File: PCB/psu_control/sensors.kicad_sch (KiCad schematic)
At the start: 35 parts

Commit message: psu_control v4 is completed
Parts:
- C11, C12, C13, C14, C15, C16: renamed from C?; footprint (none) -> Capacitor_SMD:C_0805_2012Metric
- J11, J12, J13, J14: renamed from J?; footprint (none) -> Connector_JST:JST_PH_B3B-PH-K_1x03_P2.00mm_Vertical
- R25, R26: renamed from R?; value R -> 10k; footprint (none) -> Resistor_SMD:R_0805_2012Metric
- R27, R28, R29, R30, R31, R32, R33, R34, R35, R36: renamed from R?; footprint (none) -> Resistor_SMD:R_0805_2012Metric
- SW2, SW3, SW4, SW5, SW6: renamed from SW?; footprint (none) -> Connector_JST:JST_PH_B2B-PH-K_1x02_P2.00mm_Vertical
- TH1: renamed from TH?; footprint (none) -> Connector_JST:JST_PH_B2B-PH-K_1x02_P2.00mm_Vertical
- TH2: renamed from TH?; footprint (none) -> Resistor_SMD:R_0805_2012Metric
- U5: renamed from U?; footprint (none) -> Package_SO:TSSOP-14_4.4x5mm_P0.65mm
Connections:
- net BUTTON_OTHER: now also U5.6; no longer U5.10
- net BUTTON_START: now also U5.10; no longer U5.2
- net BUTTON_STOP: now also U5.8; no longer U5.4
- net BUTTON_VOLUME_DOWN: now also U5.4; no longer U5.8
- net BUTTON_VOLUME_UP: now also U5.2; no longer U5.6
- net GND: now also SW2.1 (A), SW3.1 (A), SW4.1 (A), SW5.1 (A), SW6.1 (A); no longer SW2.2 (B), SW3.2 (B), SW4.2 (B), SW5.2 (B), SW6.2 (B)
- net at R27.2, R30.1: now also SW2.2 (B); no longer SW2.1 (A)
- net at C11.1, R30.2: now also U5.11; no longer U5.1
- net at R34.2, R36.1: now also SW6.2 (B); no longer SW6.1 (A)
- net at R28.2, R31.1: now also SW3.2 (B); no longer SW3.1 (A)
- net at C12.1, R31.2: now also U5.9; no longer U5.3
- net at R33.2, R35.1: now also SW5.2 (B); no longer SW5.1 (A)
- net at C15.1, R35.2: now also U5.3; no longer U5.9
- net at C16.1, R36.2: now also U5.5; no longer U5.11
- net at R29.2, R32.1: now also SW4.2 (B); no longer SW4.1 (A)
- net at C13.1, R32.2: now also U5.1; no longer U5.5
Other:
- note added: "J11: JST PH Connector J12: JST PH Connector J13: JST PH Connector J14: JST PH Connector"
- note added: "SW2: JST PH Connector SW3: JST PH Connector SW4: JST PH Connector SW5: JST PH Connector SW6: JST PH Connector"
- note added: "TH1: JST PH Connector TH2: 0805 SMD"
- moved on the sheet: C12, C16, J11, J13, J14, R28, R31, R34, R36, SW2, SW3, SW4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

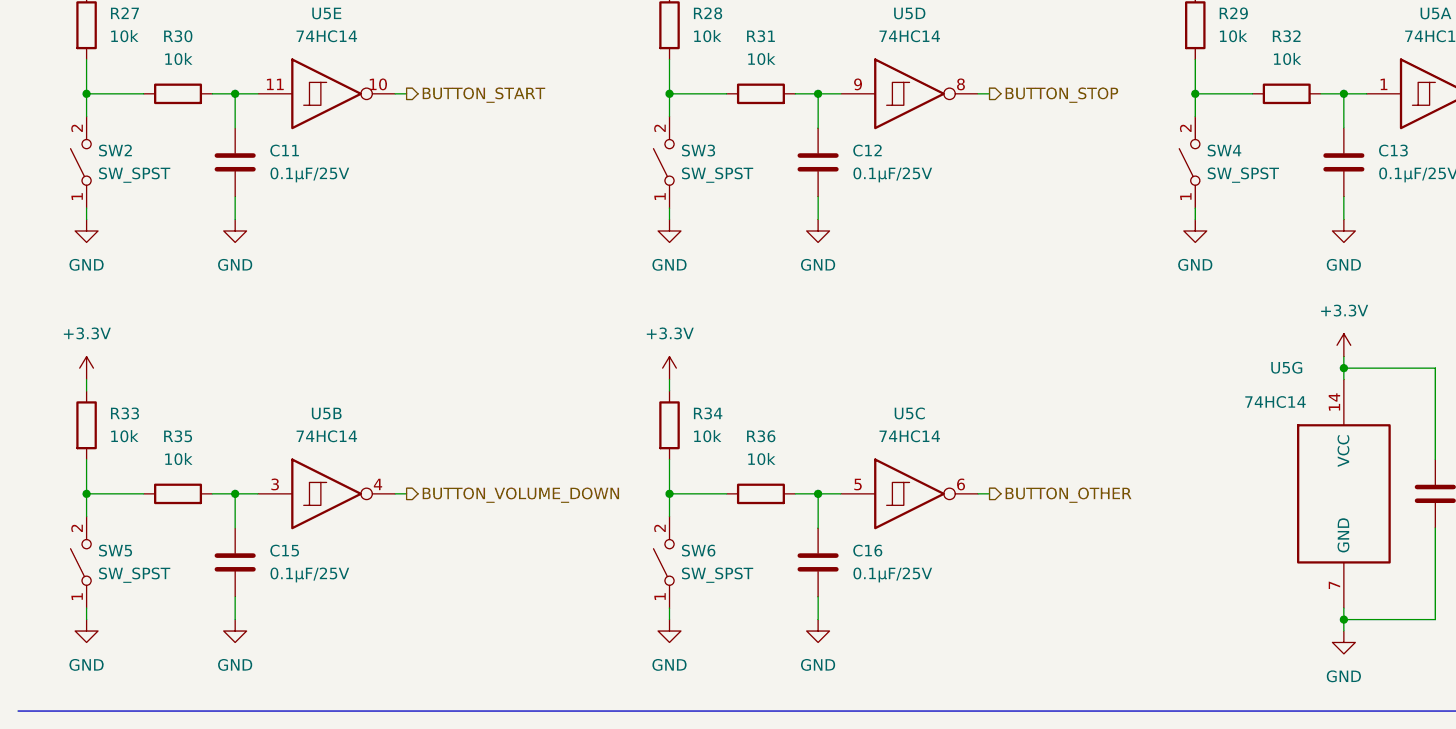
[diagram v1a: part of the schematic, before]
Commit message: Add dynamixel_control PCB
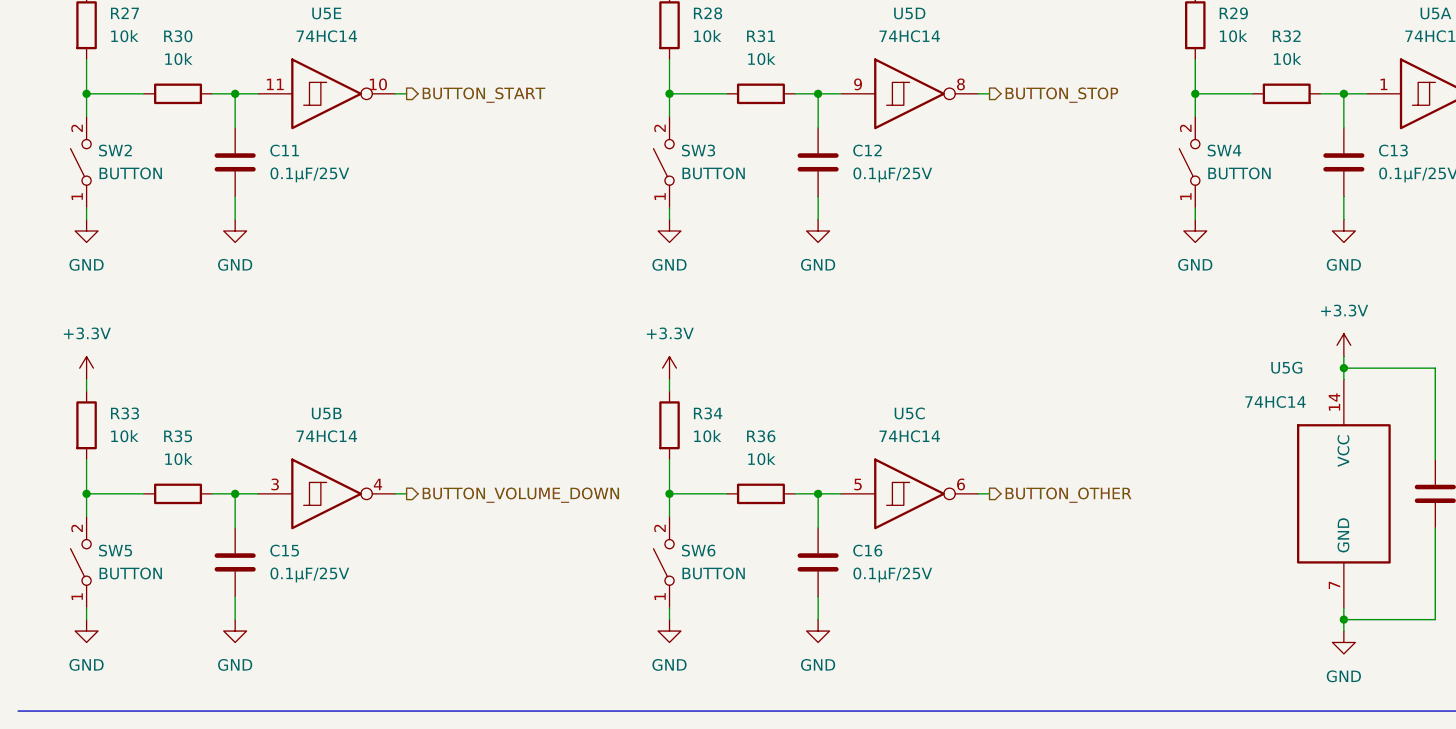
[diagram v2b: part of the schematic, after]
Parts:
- SW2, SW3, SW4, SW5, SW6: value SW_SPST -> BUTTON
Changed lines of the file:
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@@
       (effects (font (size 1.27 1.27)) (justify right))
     )
-    (property "Value" "SW_SPST" (id 1) (at 86.36 139.6999 90)
+    (property "Value" "BUTTON" (id 1) (at 86.36 139.6999 90)
       (effects (font (size 1.27 1.27)) (justify right))
     )
@@
       (effects (font (size 1.27 1.27)) (justify right))
     )
-    (property "Value" "SW_SPST" (id 1) (at 21.59 139.6999 90)
+    (property "Value" "BUTTON" (id 1) (at 21.59 139.6999 90)
       (effects (font (size 1.27 1.27)) (justify right))
     )
@@
       (effects (font (size 1.27 1.27)) (justify right))
     )
-    (property "Value" "SW_SPST" (id 1) (at 144.78 95.2499 90)
+    (property "Value" "BUTTON" (id 1) (at 144.78 95.2499 90)
       (effects (font (size 1.27 1.27)) (justify right))
     )
@@
       (effects (font (size 1.27 1.27)) (justify right))
     )
-    (property "Value" "SW_SPST" (id 1) (at 86.36 95.2499 90)
+    (property "Value" "BUTTON" (id 1) (at 86.36 95.2499 90)
       (effects (font (size 1.27 1.27)) (justify right))
     )
@@
       (effects (font (size 1.27 1.27)) (justify right))
     )
-    (property "Value" "SW_SPST" (id 1) (at 21.59 95.2499 90)
-      (effects (font (size 1.27 1.27)) (justify right))
-    )
+    (property "Value" "BUTTON" (id 1) (at 21.59 95.2499 90)
+      (effects (font (size 1.27 1.27)) (justify right))
+    )

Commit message: Fix issues. Add schematic files.
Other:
- note added: "Light Sensor Model: Adafruit 2748"
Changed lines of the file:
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@@
+    (effects (font (size 1.27 1.27)) (justify left bottom))
+  )
+  (text "Light Sensor Model: Adafruit 2748" (at 82.55 59.69 0)
     (effects (font (size 1.27 1.27)) (justify left bottom))
   )

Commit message: Fix PCBs.
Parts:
- added C25, C26, C27, C28, C29, C30: 0.1µF/25V, Capacitor_SMD:C_0805_2012Metric, symbol Device:C
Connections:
- net EXTERNAL_TEMPERATURE: now also C27.1
- net GND: now also C25.2, C26.2, C27.2, C28.2, C29.2, C30.2
- net LIGHT_SENSOR_BACK: now also C29.1
- net LIGHT_SENSOR_FRONT: now also C25.1
- net LIGHT_SENSOR_LEFT: now also C26.1
- net LIGHT_SENSOR_RIGHT: now also C30.1
- net ONBOARD_TEMPERATURE: now also C28.1
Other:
- moved on the sheet: C11, C12, C13, C14, C15, C16, J11, J12, J13, J14, R25, R26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
